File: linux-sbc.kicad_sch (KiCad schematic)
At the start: 9 parts, among them J101 Molex Mini-fit Jr

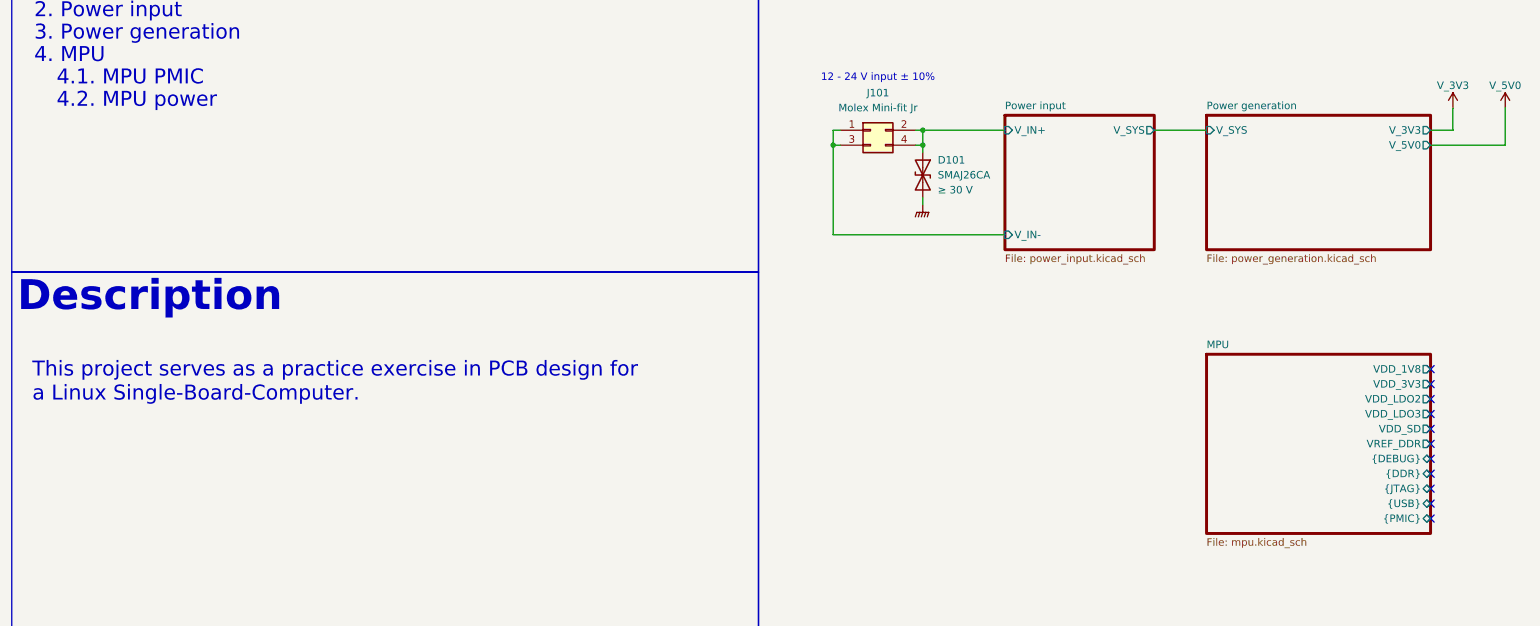
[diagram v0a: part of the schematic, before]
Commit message: Add USB-to-UART debug option
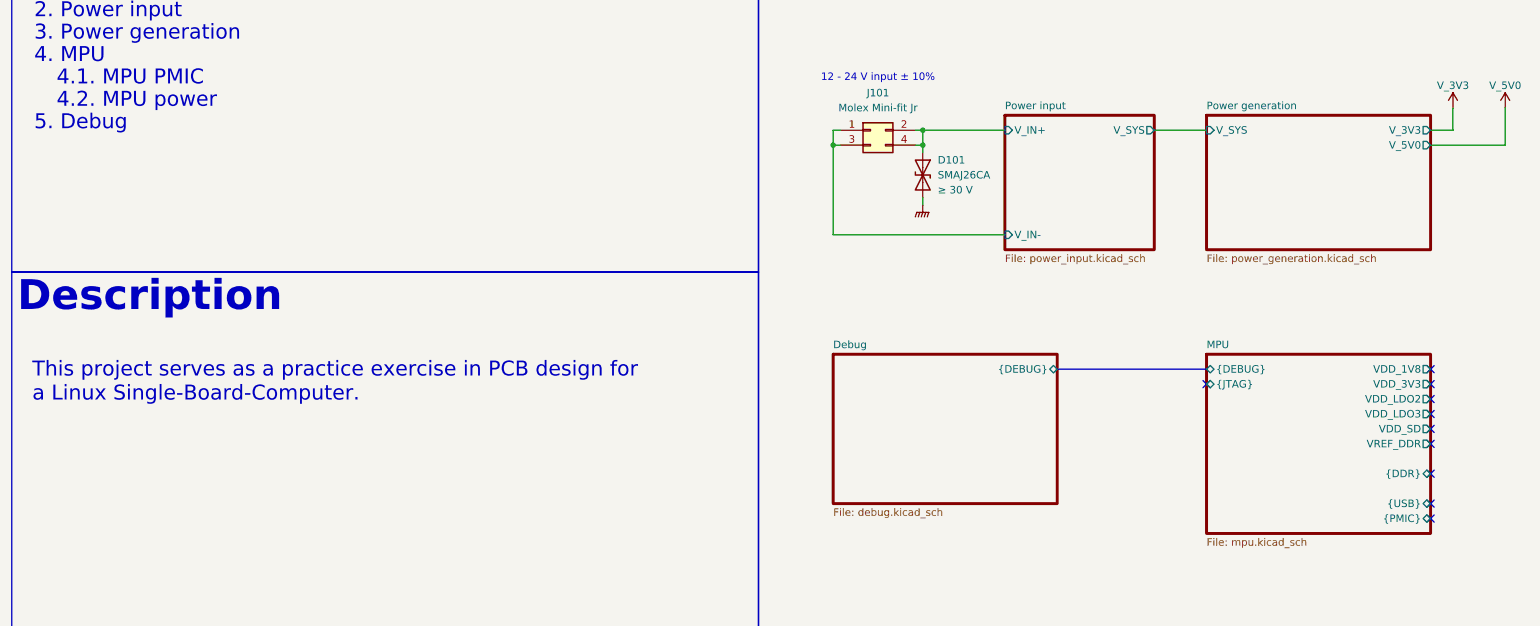
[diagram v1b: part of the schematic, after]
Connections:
- no-connect marks 11 -> 10
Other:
- added sheet Debug (debug.kicad_sch)
- note added: "5. Debug"
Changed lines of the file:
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@@
+		)
+	)
+	(text "5. Debug"
+		(exclude_from_sim no)
+		(at 16.51 87.63 0)
+		(effects
+			(font
+				(size 2.54 2.54)
+			)
+			(justify left)
+			(href "#3")
 		)
 	)
@@
 	)
 	(no_connect
-		(at 254 144.78)
+		(at 215.9 132.08)
 	)
 	(no_connect
@@
 	)
 	(no_connect
-		(at 254 149.86)
-	)
-	(no_connect
 		(at 254 147.32)
 	)
@@
 		(pts
 			(xy 167.64 91.44) (xy 167.64 92.71)
+		)
+		(stroke
+			(width 0)
+			(type default)
+		)
+	)
+	(bus
+		(pts
+			(xy 190.5 129.54) (xy 215.9 129.54)
 		)
 		(stroke
@@
 		)
 		(pin "{JTAG}" bidirectional
-			(at 254 149.86 0)
-			(effects
-				(font
-					(size 1.27 1.27)
-				)
-				(justify right)
+			(at 215.9 132.08 180)
+			(effects
+				(font
+					(size 1.27 1.27)
+				)
+				(justify left)
 			)
 		)
@@
 		)
 		(pin "{DEBUG}" bidirectional
-			(at 254 144.78 0)
-			(effects
-				(font
-					(size 1.27 1.27)
-				)
-				(justify right)
+			(at 215.9 129.54 180)
+			(effects
+				(font
+					(size 1.27 1.27)
+				)
+				(justify left)
 			)
 		)
@@
 				)
 			)
+		)
+	)
+	(sheet
+		(at 152.4 127)
+		(size 38.1 25.4)
+		(exclude_from_sim no)
+		(in_bom yes)
+		(on_board yes)
+		(dnp no)
+		(fields_autoplaced yes)
+		(stroke
+			(width 0.5)
+			(type solid)
+			(color 255 255 0 1)
+		)
+		(fill
+			(color 0 255 0 1.0000)
+		)
+		(property "Sheetname" "Debug"
+			(at 152.4 126.1146 0)
+			(effects
+				(font
+					(size 1.27 1.27)
+				)
+				(justify left bottom)
+			)
+		)
+		(property "Sheetfile" "debug.kicad_sch"
+			(at 152.4 153.1584 0)
+			(effects
+				(font
+					(size 1.27 1.27)
+				)
+				(justify left top)
+			)
+		)
+		(pin "{DEBUG}" bidirectional
+			(at 190.5 129.54 0)
+			(effects
+				(font
+					(size 1.27 1.27)
+				)
+				(justify right)
+			)
+		)
+		(instances
+			(project "linux-sbc"
+				(path "/fa11a02f-8043-4153-ab69-88d766503017"
+					(page "7")
+				)
+			)

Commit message: Add a debug section
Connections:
- no-connect marks 10 -> 8
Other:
- sheet Debug ports: added VDD, {JTAG}, {PMIC}; removed none
- sheet MPU ports: added VDD; removed none
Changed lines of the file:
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@@
 			)
 			(justify left)
-			(href "#3")
+			(href "#4")
 		)
 	)
@@
 			)
 			(justify left)
-			(href "#3")
+			(href "#7")
 		)
 	)
@@
 			)
 			(justify left)
-			(href "#4")
+			(href "#6")
 		)
 	)
@@
 			)
 			(justify left)
-			(href "#4")
+			(href "#5")
 		)
 	)
@@
 	)
 	(no_connect
+		(at 254 139.7)
+	)
+	(no_connect
+		(at 254 144.78)
+	)
+	(no_connect
 		(at 254 137.16)
 	)
 	(no_connect
-		(at 215.9 132.08)
+		(at 254 149.86)
+	)
+	(no_connect
+		(at 254 132.08)
 	)
 	(no_connect
@@
 	)
 	(no_connect
+		(at 254 152.4)
+	)
+	(no_connect
 		(at 254 134.62)
 	)
-	(no_connect
-		(at 254 147.32)
-	)
-	(no_connect
-		(at 254 129.54)
-	)
-	(no_connect
-		(at 254 139.7)
-	)
-	(no_connect
-		(at 254 154.94)
-	)
-	(no_connect
-		(at 254 152.4)
-	)
-	(no_connect
-		(at 254 132.08)
-	)
 	(wire
 		(pts
@@
 		)
 	)
+	(bus
+		(pts
+			(xy 254 162.56) (xy 292.1 162.56)
+		)
+		(stroke
+			(width 0)
+			(type default)
+		)
+	)
 	(wire
 		(pts
@@
 	(wire
 		(pts
+			(xy 289.56 142.24) (xy 292.1 142.24)
+		)
+		(stroke
+			(width 0)
+			(type default)
+		)
+	)
+	(wire
+		(pts
 			(xy 167.64 88.9) (xy 167.64 91.44)
 		)
@@
 	(wire
 		(pts
+			(xy 289.56 129.54) (xy 289.56 142.24)
+		)
+		(stroke
+			(width 0)
+			(type default)
+		)
+	)
+	(wire
+		(pts
 			(xy 166.37 88.9) (xy 167.64 88.9)
 		)
@@
 		)
 	)
+	(bus
+		(pts
+			(xy 254 160.02) (xy 292.1 160.02)
+		)
+		(stroke
+			(width 0)
+			(type default)
+		)
+	)
+	(bus
+		(pts
+			(xy 254 157.48) (xy 292.1 157.48)
+		)
+		(stroke
+			(width 0)
+			(type default)
+		)
+	)
 	(wire
 		(pts
@@
 		)
 	)
-	(bus
-		(pts
-			(xy 190.5 129.54) (xy 215.9 129.54)
+	(wire
+		(pts
+			(xy 254 129.54) (xy 289.56 129.54)
 		)
 		(stroke
@@
 	(sheet
 		(at 215.9 127)
-		(size 38.1 30.48)
+		(size 38.1 38.1)
 		(exclude_from_sim no)
 		(in_bom yes)
@@
 		)
 		(property "Sheetfile" "mpu.kicad_sch"
-			(at 215.9 158.2384 0)
+			(at 215.9 165.8584 0)
 			(effects
 				(font
@@
 		)
 		(pin "{DDR}" bidirectional
-			(at 254 147.32 0)
+			(at 254 149.86 0)
 			(effects
 				(font
@@
 		)
 		(pin "{JTAG}" bidirectional
-			(at 215.9 132.08 180)
-			(effects
-				(font
-					(size 1.27 1.27)
-				)
-				(justify left)
+			(at 254 162.56 0)
+			(effects
+				(font
+					(size 1.27 1.27)
+				)
+				(justify right)
 			)
 		)
@@
 		)
 		(pin "VDD_1V8" output
+			(at 254 132.08 0)
+			(effects
+				(font
+					(size 1.27 1.27)
+				)
+				(justify right)
+			)
+		)
+		(pin "VDD_3V3" output
+			(at 254 134.62 0)
+			(effects
+				(font
+					(size 1.27 1.27)
+				)
+				(justify right)
+			)
+		)
+		(pin "VDD_LDO2" output
+			(at 254 137.16 0)
+			(effects
+				(font
+					(size 1.27 1.27)
+				)
+				(justify right)
+			)
+		)
+		(pin "VDD_LDO3" output
+			(at 254 139.7 0)
+			(effects
+				(font
+					(size 1.27 1.27)
+				)
+				(justify right)
+			)
+		)
+		(pin "VDD_SD" output
+			(at 254 142.24 0)
+			(effects
+				(font
+					(size 1.27 1.27)
+				)
+				(justify right)
+			)
+		)
+		(pin "VREF_DDR" output
+			(at 254 144.78 0)
+			(effects
+				(font
+					(size 1.27 1.27)
+				)
+				(justify right)
+			)
+		)
+		(pin "{PMIC}" bidirectional
+			(at 254 157.48 0)
+			(effects
+				(font
+					(size 1.27 1.27)
+				)
+				(justify right)
+			)
+		)
+		(pin "{DEBUG}" bidirectional
+			(at 254 160.02 0)
+			(effects
+				(font
+					(size 1.27 1.27)
+				)
+				(justify right)
+			)
+		)
+		(pin "VDD" output
 			(at 254 129.54 0)
 			(effects
@@
 				)
 				(justify right)
-			)
-		)
-		(pin "VDD_3V3" output
-			(at 254 132.08 0)
-			(effects
-				(font
-					(size 1.27 1.27)
-				)
-				(justify right)
-			)
-		)
-		(pin "VDD_LDO2" output
-			(at 254 134.62 0)
-			(effects
-				(font
-					(size 1.27 1.27)
-				)
-				(justify right)
-			)
-		)
-		(pin "VDD_LDO3" output
-			(at 254 137.16 0)
-			(effects
-				(font
-					(size 1.27 1.27)
-				)
-				(justify right)
-			)
-		)
-		(pin "VDD_SD" output
-			(at 254 139.7 0)
-			(effects
-				(font
-					(size 1.27 1.27)
-				)
-				(justify right)
-			)
-		)
-		(pin "VREF_DDR" output
-			(at 254 142.24 0)
-			(effects
-				(font
-					(size 1.27 1.27)
-				)
-				(justify right)
-			)
-		)
-		(pin "{PMIC}" bidirectional
-			(at 254 154.94 0)
-			(effects
-				(font
-					(size 1.27 1.27)
-				)
-				(justify right)
-			)
-		)
-		(pin "{DEBUG}" bidirectional
-			(at 215.9 129.54 180)
-			(effects
-				(font
-					(size 1.27 1.27)
-				)
-				(justify left)
 			)
 		)
@@
 	)
 	(sheet
-		(at 152.4 127)
+		(at 292.1 139.7)
 		(size 38.1 25.4)
 		(exclude_from_sim no)
@@
 		)
 		(property "Sheetname" "Debug"
-			(at 152.4 126.1146 0)
+			(at 292.1 138.8146 0)
 			(effects
 				(font
@@
 		)
 		(property "Sheetfile" "debug.kicad_sch"
-			(at 152.4 153.1584 0)
+			(at 292.1 165.8584 0)
 			(effects
 				(font
@@
 		)
 		(pin "{DEBUG}" bidirectional
-			(at 190.5 129.54 0)
-			(effects
-				(font
-					(size 1.27 1.27)
-				)
-				(justify right)
-			)
-		)
+			(at 292.1 160.02 180)
+			(effects
+				(font
+					(size 1.27 1.27)
+				)
+				(justify left)
+			)
+		)
+		(pin "VDD" input
+			(at 292.1 142.24 180)
+			(effects
+				(font
+					(size 1.27 1.27)
+				)
+				(justify left)
+			)
+		)
+		(pin "{JTAG}" bidirectional
+			(at 292.1 162.56 180)
+			(effects
+				(font
+					(size 1.27 1.27)
+				)
+				(justify left)
+			)
+		)
+		(pin "{PMIC}" bidirectional
+			(at 292.1 157.48 180)
+			(effects
+				(font
+					(size 1.27 1.27)
+				)
+				(justify left)
+			)
+		)

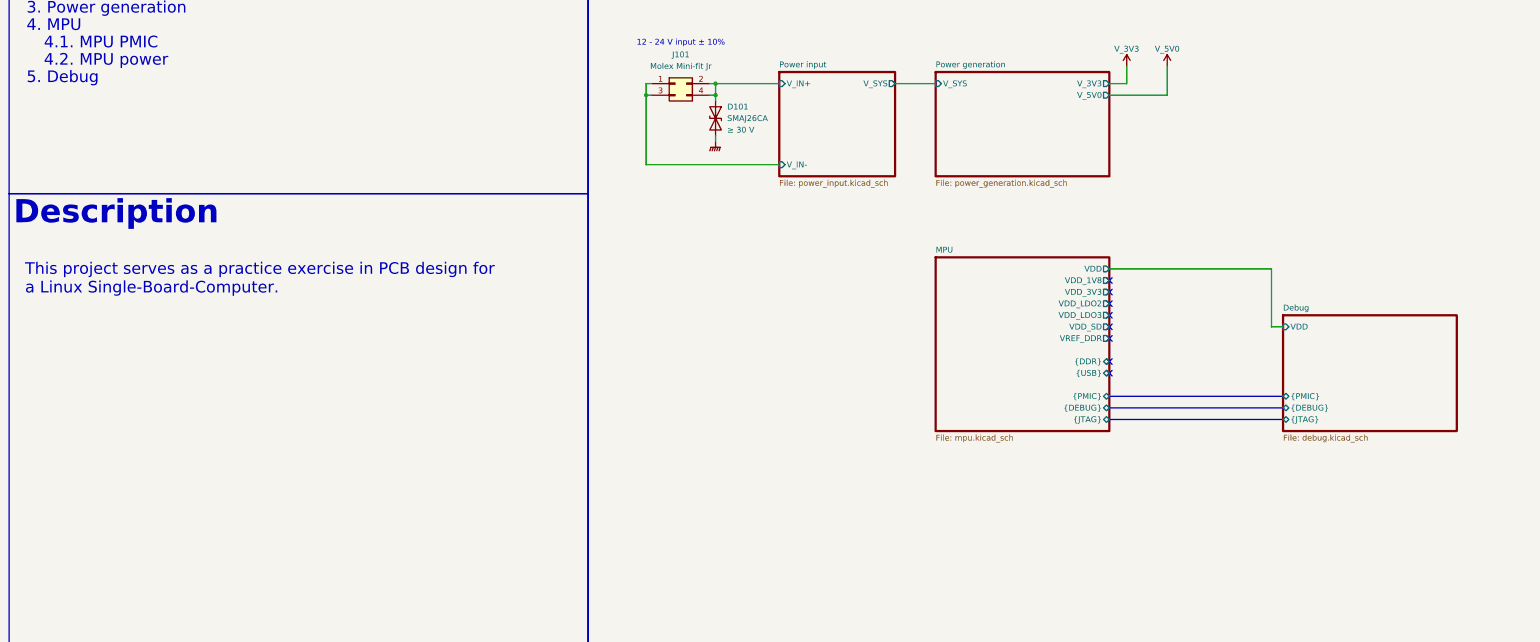
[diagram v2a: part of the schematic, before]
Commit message: Add DDR page
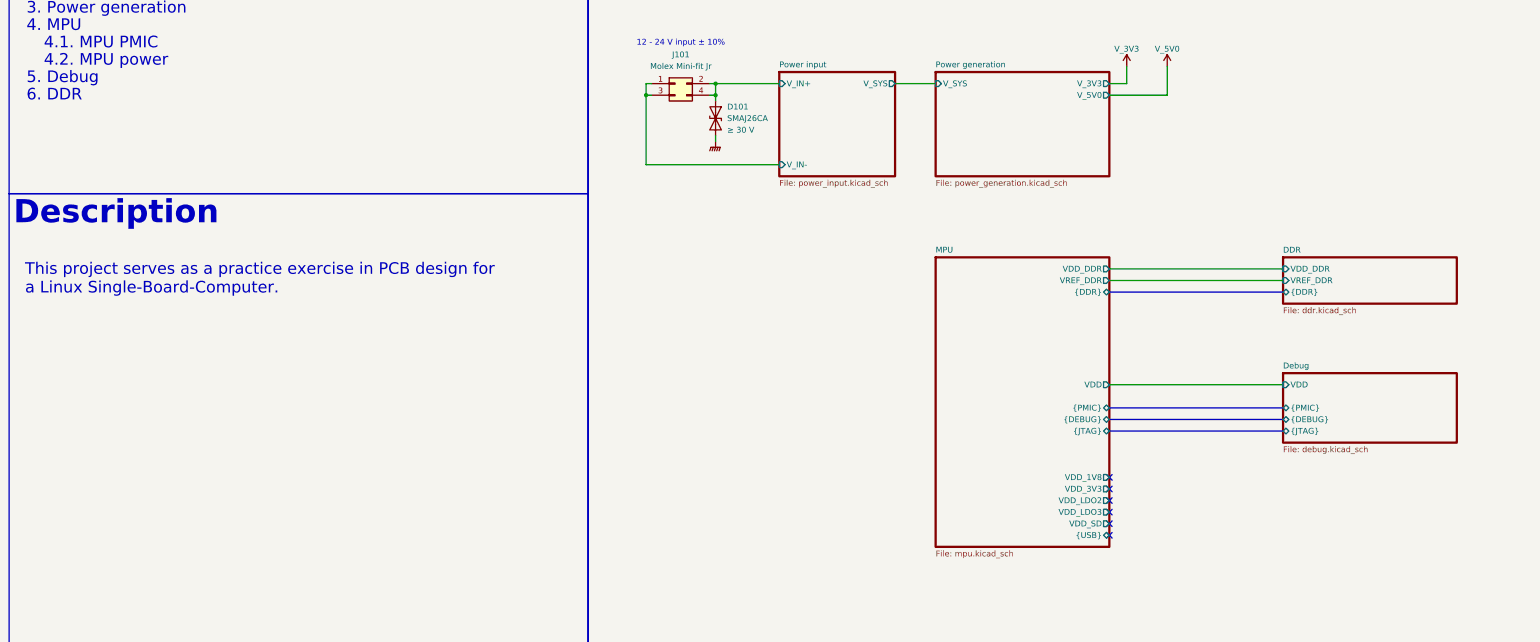
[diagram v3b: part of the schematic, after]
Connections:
- no-connect marks 8 -> 6
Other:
- added sheet DDR (ddr.kicad_sch)
- sheet MPU ports: added VDD_DDR; removed none
- note added: "6. DDR"
